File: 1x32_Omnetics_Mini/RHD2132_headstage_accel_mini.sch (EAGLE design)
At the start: 18 parts, among them U1 RHD2132_QFN, U2 ADXL335

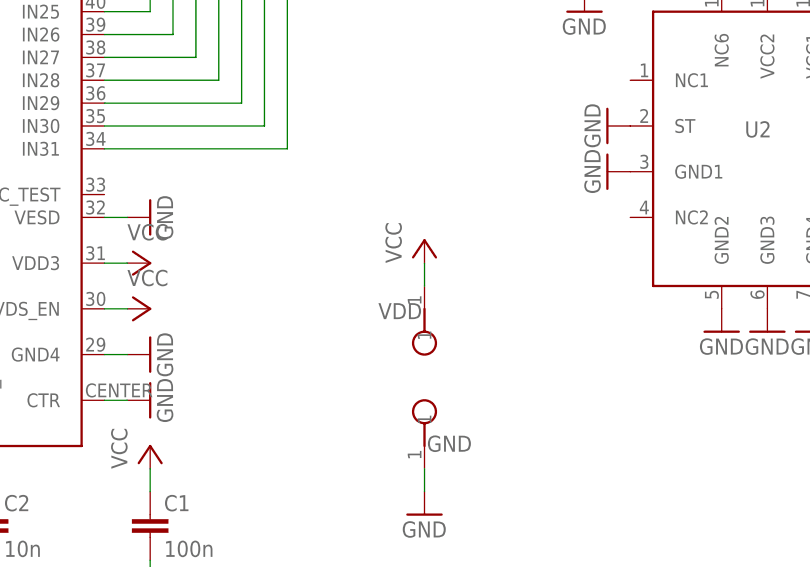
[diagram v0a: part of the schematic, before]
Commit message: started some routing
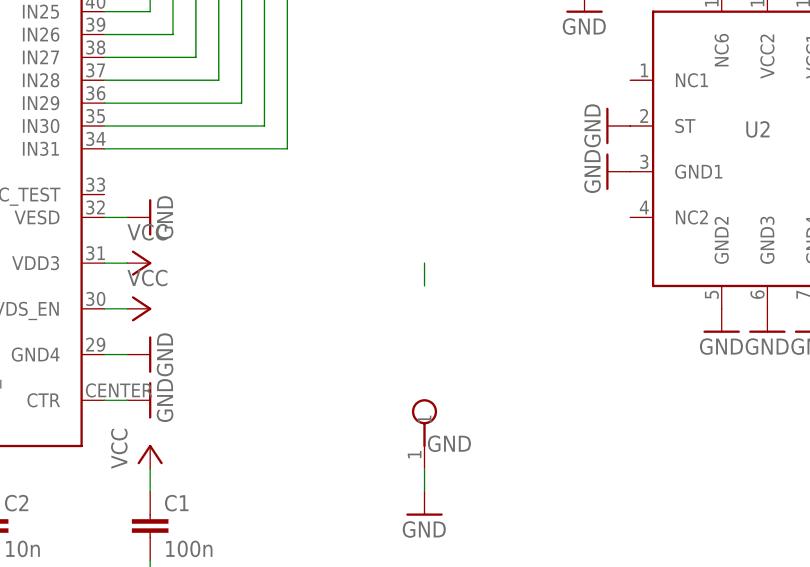
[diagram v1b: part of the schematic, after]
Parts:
- removed VDD: TESTPOINT_SMALL, RHD2000_eval_board:TESTPOINT_SMALL
- C1, C2, C3, CX, CY, CZ: device RHD2000_eval_board:C_0402 -> RHD2000_eval_board:C_0201
- R0, R1, R2, R3: device RHD2000_eval_board:R_0402 -> RHD2000_eval_board:R_0201
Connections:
- net VCC: no longer VDD.1
